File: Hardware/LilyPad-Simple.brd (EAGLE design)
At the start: 50 x 50 mm, 43 parts, among them U1 ATMEGA328P_TQFP, U2 MCP73831, U3 MIC5219 3.3V, Y1 8MHZ

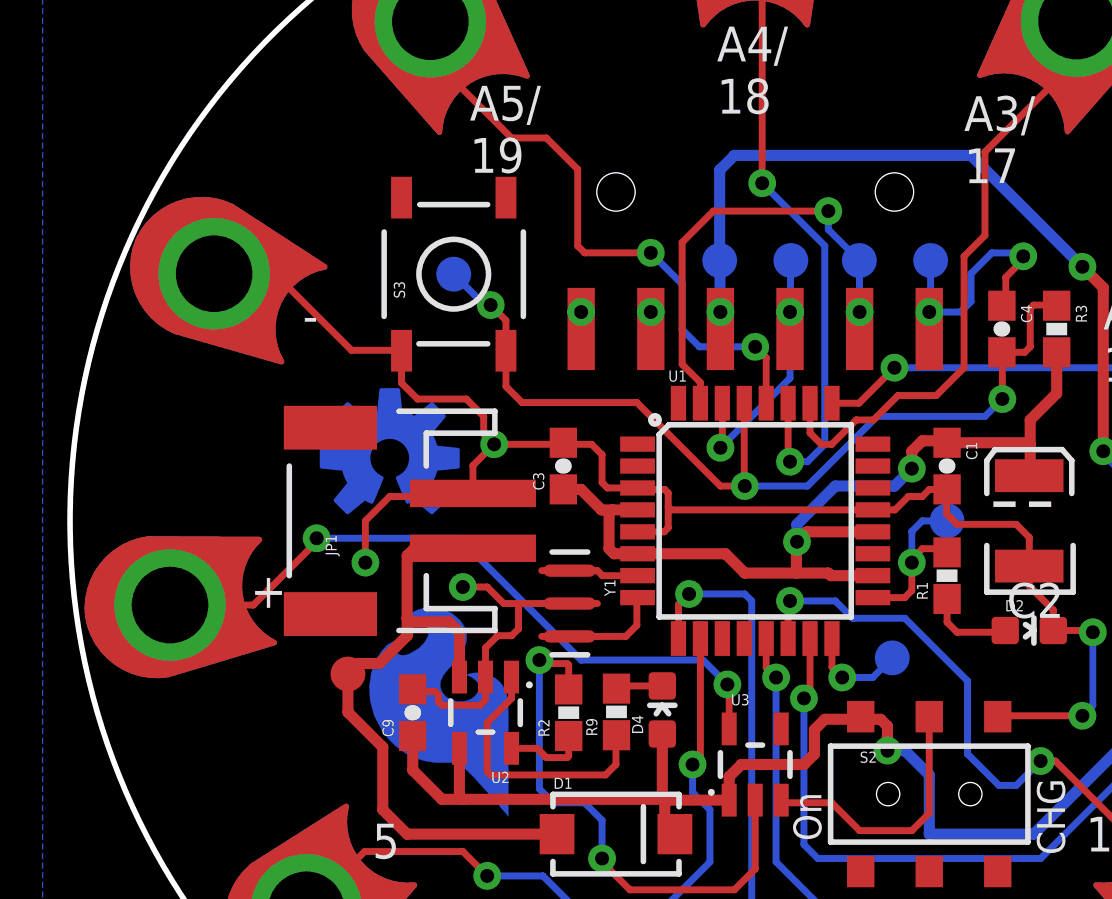
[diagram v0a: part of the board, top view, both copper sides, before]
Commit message: Put test pads on grid, increased trace size on power supply pad
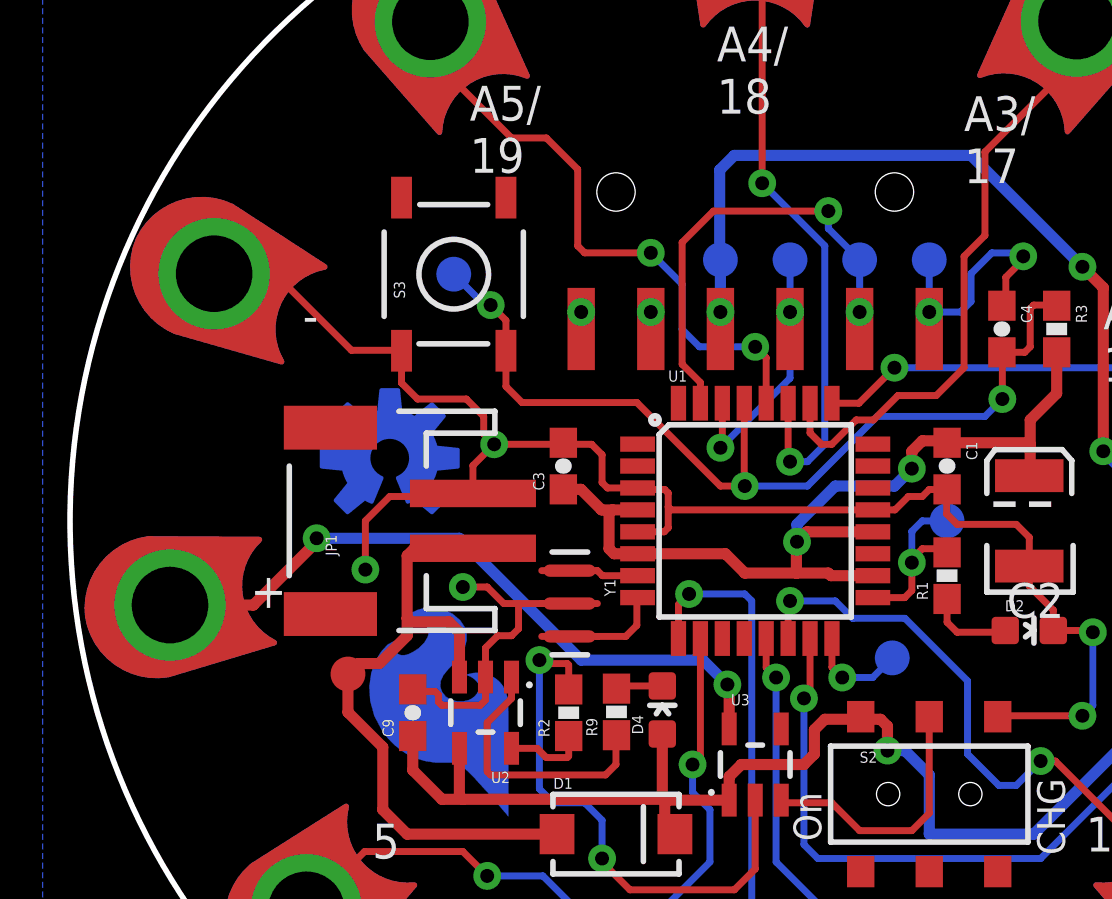
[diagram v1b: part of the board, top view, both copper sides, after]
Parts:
- moved TP-DTR 0.06 mm to (6.35, 9.53)
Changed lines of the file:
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@@
 <layer number="47" name="Measures" color="7" fill="1" visible="no" active="yes"/>
 <layer number="48" name="Document" color="7" fill="1" visible="no" active="yes"/>
-<layer number="49" name="Reference" color="7" fill="1" visible="yes" active="yes"/>
+<layer number="49" name="Reference" color="7" fill="1" visible="no" active="yes"/>
 <layer number="50" name="dxf" color="7" fill="1" visible="no" active="yes"/>
 <layer number="51" name="tDocu" color="6" fill="1" visible="yes" active="yes"/>
@@
 <attribute name="PROD_ID" value="SWCH-08179" x="6.35" y="-9.97" size="1.778" layer="27" display="off"/>
 </element>
-<element name="TP-TX" library="SparkFun" package="PAD.03X.05" value="" x="3.8" y="9.5" rot="MR90"/>
-<element name="TP-RX" library="SparkFun" package="PAD.03X.05" value="" x="1.3" y="9.5" rot="MR0"/>
-<element name="TP-DTR" library="SparkFun" package="PAD.03X.05" value="" x="6.4" y="9.5" rot="MR0"/>
+<element name="TP-TX" library="SparkFun" package="PAD.03X.05" value="" x="3.81" y="9.525" rot="MR90"/>
+<element name="TP-RX" library="SparkFun" package="PAD.03X.05" value="" x="1.27" y="9.525" rot="MR0"/>
+<element name="TP-DTR" library="SparkFun" package="PAD.03X.05" value="" x="6.35" y="9.525" rot="MR0"/>
 <element name="C9" library="SparkFun-Capacitors" package="0603-CAP" value="4.7uF" x="-12.495" y="-7" smashed="yes" rot="R90">
 <attribute name="NAME" x="-13.1935" y="-7.889" size="0.4064" layer="25" rot="R90"/>
@@
 <attribute name="PROD_ID" value="RES-00824" x="-6.806" y="-7" size="1.778" layer="27" rot="R90" display="off"/>
 </element>
-<element name="TP-FTDI_VCC" library="SparkFun" package="PAD.03X.05" value="" x="-1.2954" y="9.4996" rot="MR0"/>
+<element name="TP-FTDI_VCC" library="SparkFun" package="PAD.03X.05" value="" x="-1.27" y="9.525" rot="MR0"/>
 <element name="LOGO2" library="SparkFun-Aesthetics" package="SFE_LOGO_FLAME_COPPER_.3" value="SFE_LOGO_FLAME.3COP" x="-8.509" y="-10.922" rot="MR0"/>
 <element name="LOGO1" library="SparkFun-Aesthetics" package="OSHW-LOGO-M_COPPER" value="OSHW-LOGOM-COPPER" x="-13.335" y="2.286" rot="MR0"/>
@@
 <wire x1="6.35" y1="1.143" x2="6.993" y2="1.143" width="0.254" layer="1"/>
 <wire x1="6.993" y1="1.143" x2="7" y2="1.15" width="0.254" layer="1"/>
-<via x="-14.224" y="-1.524" extent="1-16" drill="0.508"/>
+<via x="-14.224" y="-1.778" extent="1-16" drill="0.508"/>
 <wire x1="-14.224" y1="0" x2="-13.335" y2="0.889" width="0.254" layer="1"/>
 <wire x1="-13.335" y1="0.889" x2="-10.411" y2="0.889" width="0.254" layer="1"/>
@@
 <wire x1="-9.779" y1="-2.413" x2="-10.668" y2="-2.413" width="0.254" layer="1"/>
 <wire x1="-8.636" y1="-3.937" x2="-8.636" y2="-3.016" width="0.254" layer="1"/>
-<wire x1="-14.224" y1="-1.524" x2="-14.224" y2="0" width="0.254" layer="1"/>
+<wire x1="-14.224" y1="-1.778" x2="-14.224" y2="0" width="0.254" layer="1"/>
 <wire x1="-6.806" y1="-6.15" x2="-6.806" y2="-5.259" width="0.254" layer="1"/>
 <wire x1="-6.806" y1="-5.259" x2="-6.858" y2="-5.207" width="0.254" layer="1"/>
@@
 <contactref element="U1" pad="30"/>
 <contactref element="TP-RX" pad="P$1"/>
-<wire x1="1.3" y1="9.5" x2="1.27" y2="7.62" width="0.254" layer="16"/>
 <via x="1.27" y="7.62" extent="1-16" drill="0.508"/>
 <via x="-1.27" y="2.667" extent="1-16" drill="0.508"/>
@@
 <wire x1="-1.2" y1="4.2926" x2="-1.2" y2="2.737" width="0.254" layer="1"/>
 <wire x1="-1.2" y1="2.737" x2="-1.27" y2="2.667" width="0.254" layer="1"/>
+<wire x1="1.27" y1="9.525" x2="1.27" y2="7.62" width="0.254" layer="16"/>
 </signal>
 <signal name="TXO">
@@
 <wire x1="-1.524" y1="11.303" x2="2.667" y2="11.303" width="0.254" layer="1"/>
 <via x="2.667" y="11.303" extent="1-16" drill="0.508"/>
-<wire x1="2.667" y1="11.303" x2="2.667" y2="10.633" width="0.254" layer="16"/>
-<wire x1="3.8" y1="9.5" x2="2.667" y2="10.633" width="0.254" layer="16"/>
-<wire x1="3.8" y1="9.5" x2="3.81" y2="7.62" width="0.254" layer="16"/>
 <via x="3.81" y="7.62" extent="1-16" drill="0.508"/>
 <wire x1="3.81" y1="7" x2="3.81" y2="7.62" width="0.254" layer="1"/>
+<wire x1="3.8" y1="7.63" x2="3.81" y2="7.62" width="0.254" layer="16"/>
+<wire x1="3.81" y1="9.525" x2="3.81" y2="7.62" width="0.254" layer="16"/>
+<wire x1="2.667" y1="11.303" x2="2.667" y2="10.668" width="0.254" layer="16"/>
+<wire x1="2.667" y1="10.668" x2="3.81" y2="9.525" width="0.254" layer="16"/>
 </signal>
 <signal name="D5">
@@
 <contactref element="JP2" pad="1"/>
 <contactref element="TP-DTR" pad="P$1"/>
-<wire x1="6.4" y1="9.5" x2="6.4" y2="7.67" width="0.254" layer="16"/>
 <wire x1="6.4" y1="7.67" x2="6.35" y2="7.62" width="0.254" layer="16"/>
 <via x="6.35" y="7.62" extent="1-16" drill="0.508"/>
@@
 <wire x1="9.144" y1="7.994" x2="9" y2="7.85" width="0.254" layer="1"/>
 <wire x1="6.35" y1="7" x2="6.35" y2="7.62" width="0.254" layer="1"/>
+<wire x1="6.35" y1="9.525" x2="6.35" y2="7.62" width="0.254" layer="16"/>
 </signal>
 <signal name="D6">
@@
 <contactref element="D1" pad="C"/>
 <wire x1="-10.795" y1="-8.3041" x2="-10.791" y2="-8.3001" width="0.254" layer="1"/>
-<wire x1="-1.2954" y1="9.4996" x2="-1.27" y2="7.62" width="0.4064" layer="16"/>
 <via x="-1.27" y="7.62" extent="1-16" drill="0.508"/>
 <wire x1="3.756" y1="-7.239" x2="4.572" y2="-7.239" width="0.4064" layer="1"/>
@@
 <wire x1="12.7" y1="2.54" x2="12.7" y2="8.509" width="0.4064" layer="1"/>
 <wire x1="12.7" y1="8.509" x2="11.938" y2="9.271" width="0.4064" layer="1"/>
-<wire x1="-1.2954" y1="9.4996" x2="-1.2954" y2="12.8016" width="0.4064" layer="16"/>
 <wire x1="-1.2954" y1="12.8016" x2="-0.762" y2="13.335" width="0.4064" layer="16"/>
 <wire x1="-0.762" y1="13.335" x2="7.874" y2="13.335" width="0.4064" layer="16"/>
@@
 <wire x1="10.16" y1="-11.43" x2="13.462" y2="-8.128" width="0.4064" layer="16"/>
 <wire x1="13.462" y1="1.778" x2="13.462" y2="-8.128" width="0.4064" layer="16"/>
+<wire x1="-1.27" y1="9.525" x2="-1.27" y2="7.62" width="0.4064" layer="16"/>
+<wire x1="-1.2954" y1="12.8016" x2="-1.2954" y2="9.5504" width="0.4064" layer="16"/>
+<wire x1="-1.2954" y1="9.5504" x2="-1.27" y2="9.525" width="0.254" layer="16"/>
 </signal>
 <signal name="V_BATT">
@@
 <contactref element="U3" pad="5"/>
 <contactref element="U$45" pad="1"/>
-<wire x1="-21.35230625" y1="-3.07171875" x2="-18.31171875" y2="-3.07171875" width="0.254" layer="1"/>
+<wire x1="-21.35230625" y1="-3.07171875" x2="-18.31171875" y2="-3.07171875" width="0.4064" layer="1"/>
 <via x="-16.002" y="-0.635" extent="1-16" drill="0.508"/>
-<wire x1="-10.795" y1="-0.635" x2="-6.35" y2="-5.08" width="0.254" layer="16"/>
-<wire x1="-6.35" y1="-5.08" x2="-1.905" y2="-5.08" width="0.254" layer="16"/>
-<wire x1="-1.905" y1="-5.08" x2="-1.016" y2="-5.969" width="0.254" layer="16"/>
+<wire x1="-1.905" y1="-5.08" x2="-1.016" y2="-5.969" width="0.4064" layer="16"/>
 <via x="-1.016" y="-5.969" extent="1-16" drill="0.508"/>
 <wire x1="-16.002" y1="-0.635" x2="-16.002" y2="-0.762" width="0.254" layer="1"/>
-<wire x1="-16.002" y1="-0.762" x2="-18.31171875" y2="-3.07171875" width="0.254" layer="1"/>
-<wire x1="-16.002" y1="-0.635" x2="-10.795" y2="-0.635" width="0.254" layer="16"/>
-<wire x1="-0.95" y1="-7.5899" x2="-0.95" y2="-6.035" width="0.254" layer="1"/>
+<wire x1="-16.002" y1="-0.762" x2="-18.31171875" y2="-3.07171875" width="0.4064" layer="1"/>
+<wire x1="-16.002" y1="-0.635" x2="-10.795" y2="-0.635" width="0.4064" layer="16"/>
+<wire x1="-0.95" y1="-7.5899" x2="-0.95" y2="-6.035" width="0.4064" layer="1"/>
 <wire x1="-0.95" y1="-6.035" x2="-1.016" y2="-5.969" width="0.254" layer="1"/>
+<wire x1="-1.905" y1="-5.08" x2="-6.35" y2="-5.08" width="0.4064" layer="16"/>
+<wire x1="-6.35" y1="-5.08" x2="-10.795" y2="-0.635" width="0.4064" layer="16"/>
 </signal>
 <signal name="N$5">

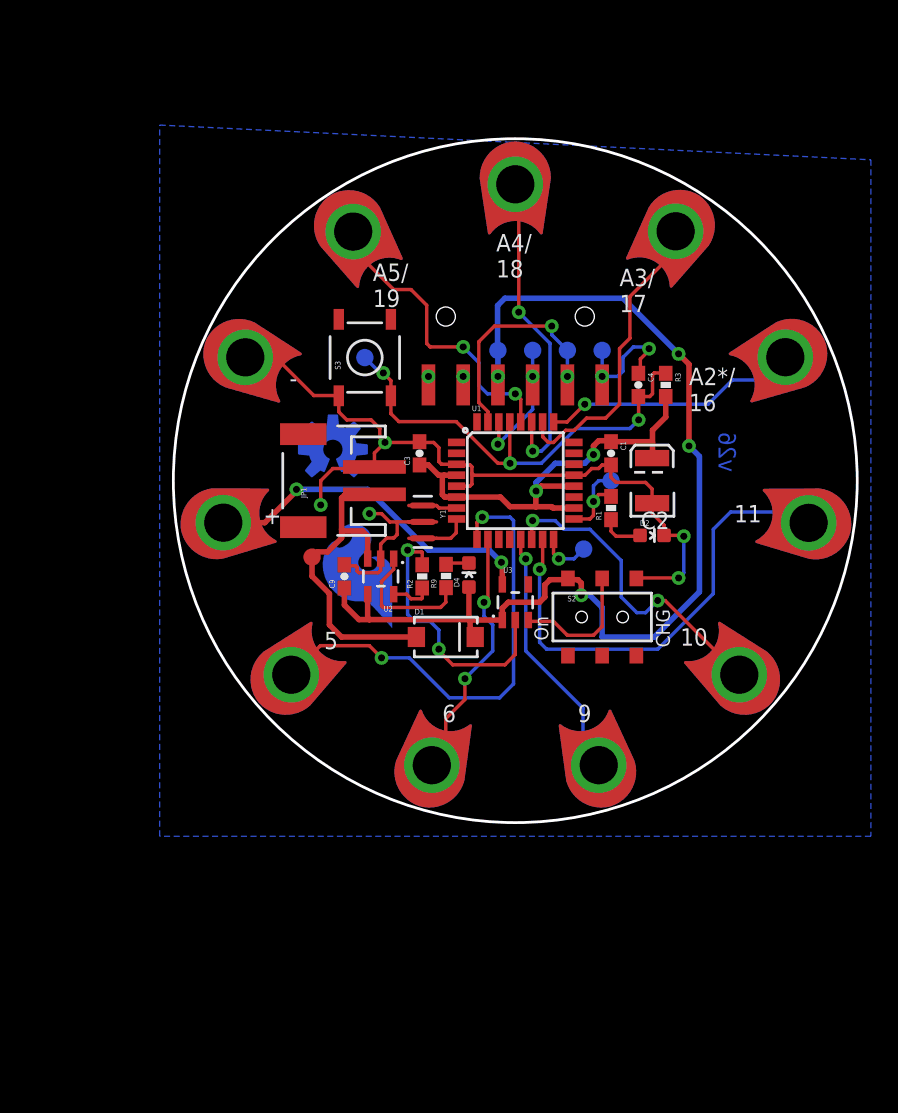
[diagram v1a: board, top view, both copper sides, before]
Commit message: DRC changes, fixed some errors
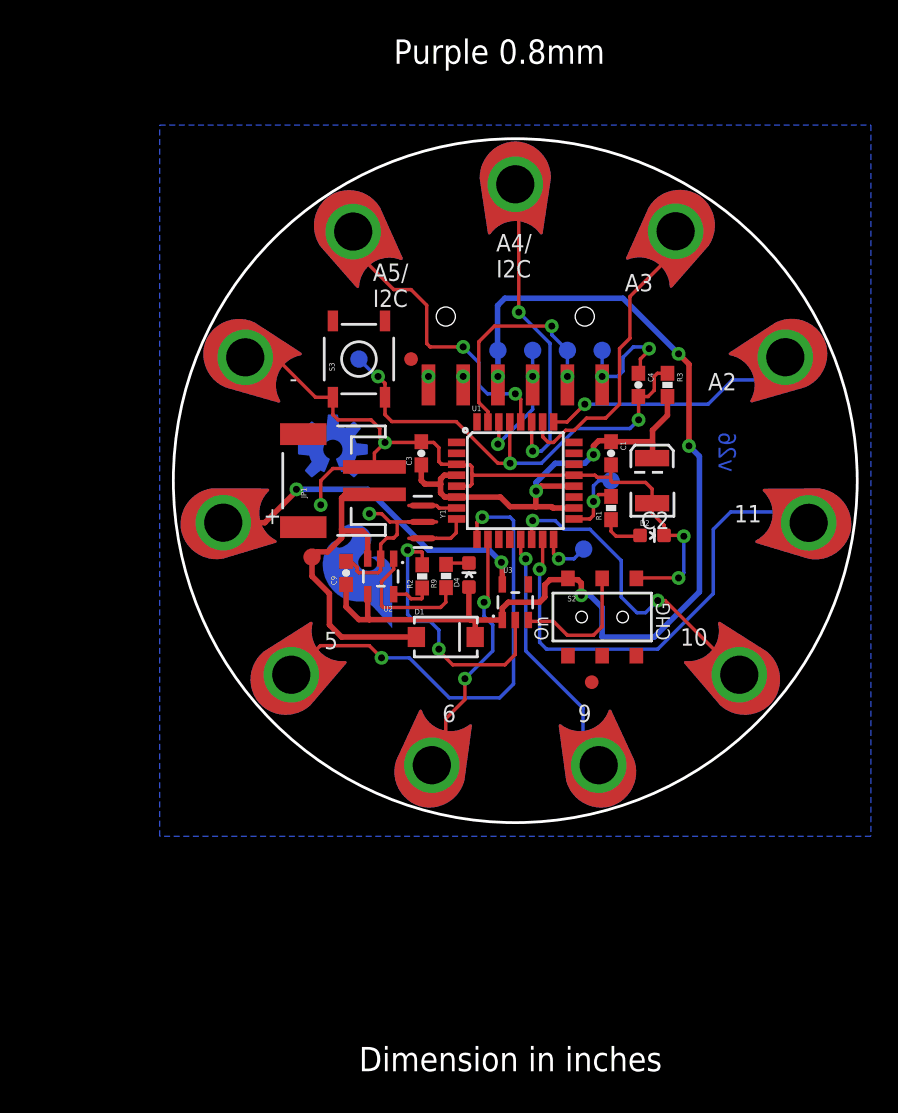
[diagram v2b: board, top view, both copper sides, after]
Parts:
- added FID1, FID2: FIDUCIAL1X2, SparkFun-Aesthetics:FIDUCIAL-1X2
- added U$2: LOGO-LPLPA, LilyPad-Wearables:LOGO-LPA
- D4: value Yellow -> RED
- moved PP-RST 0.44 mm to (-11.4, 8.89)
- moved S3 0.44 mm to (-11.4, 8.89)
- moved C9 0.28 mm to (-12.4, -6.75)
- moved R3 0.13 mm to (11.1, 7.00)
- moved C3 0.13 mm to (-6.87, 2.00)
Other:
- board text added: "A2"
- board text added: "A3"
- board text added: "A4/ I2C"
- board text added: "A5/ I2C"
- board text added: "Dimension in inches"
- board text added: "Purple 0.8mm"
- board text removed: "A2*/ 16"
- board text removed: "A3/ 17"
- board text removed: "A4/ 18"
- board text removed: "A5/ 19"

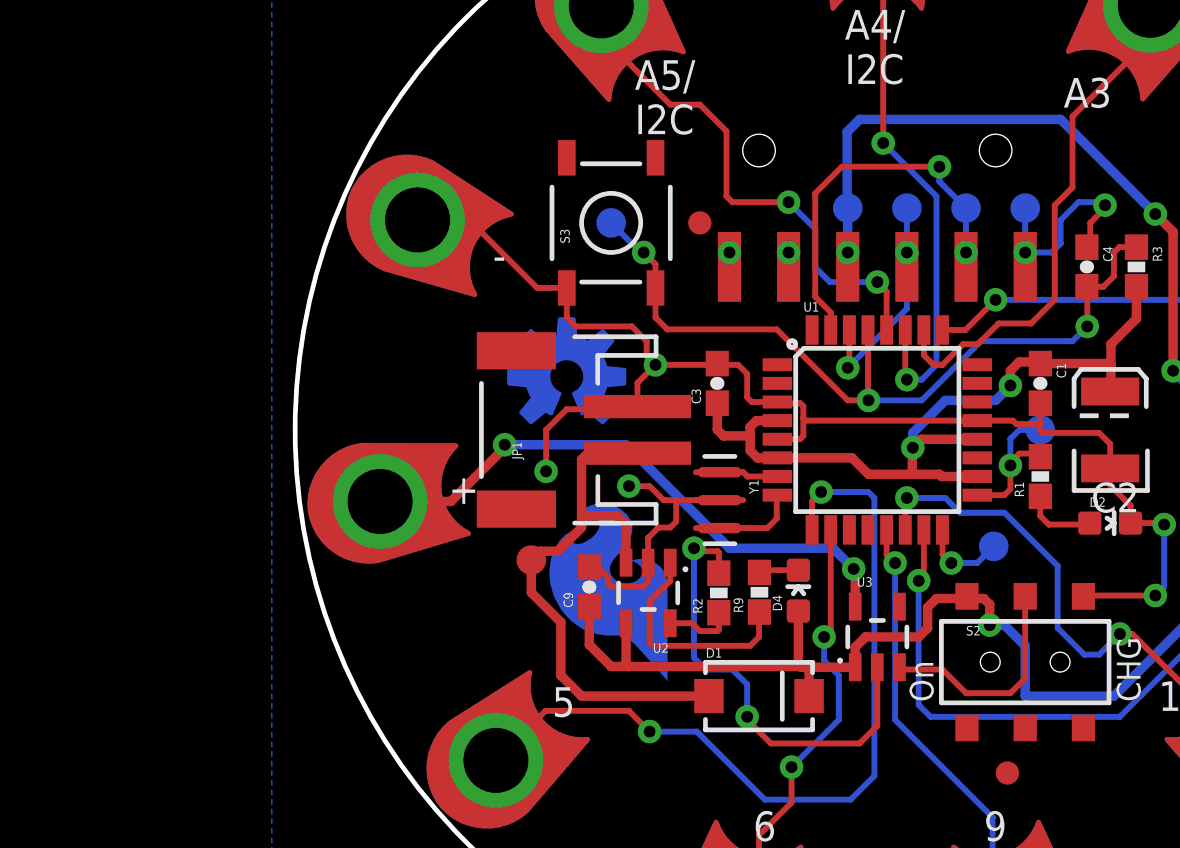
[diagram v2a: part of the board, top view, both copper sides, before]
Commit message: Change to 3.3v connections
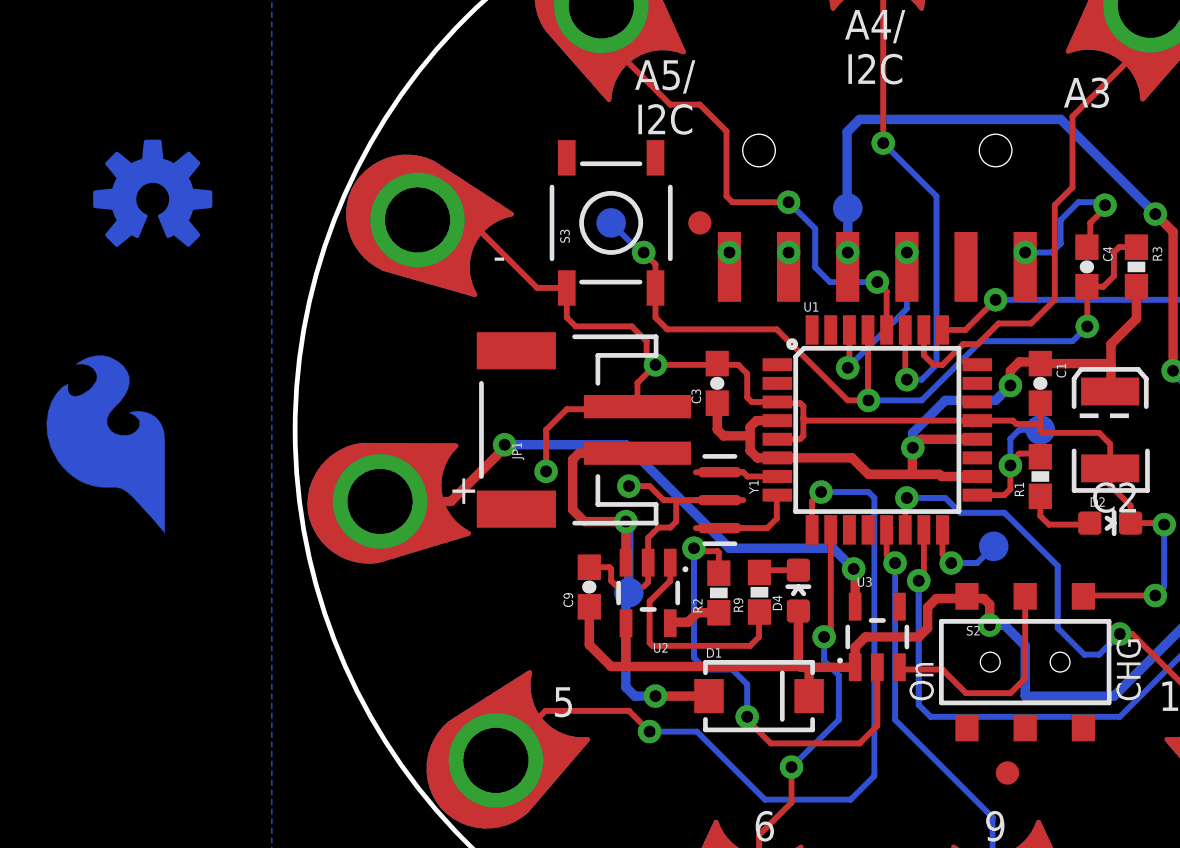
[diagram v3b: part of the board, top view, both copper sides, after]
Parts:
- removed TP-DTR, TP-RX, TP-TX: (no value), SparkFun:PAD.03X.05
- moved LOGO2 22.5 mm to (-30.1, -4.57)
- moved LOGO1 19.3 mm to (-31.1, 9.91)
- moved TP-VBATT1 4.42 mm to (-10.7, -6.99), flipped to the bottom
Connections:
- removed net VCC: C1.1, C2.A, C3.1, R3.2, U1.18, U1.20, U1.4, U1.6
- net 3.3V: now also C1.1, C2.A, C3.1, R3.2, U1.18, U1.20, U1.4, U1.6
- net DTR: no longer JP2.1, TP-DTR.P$1
- net RXI: no longer JP2.3, TP-RX.P$1
- net TXO: no longer JP2.2, TP-TX.P$1
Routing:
- net VCC: track 35.0 -> 0.00 mm, vias 2 -> 0
- net 3.3V: track 25.3 -> 60.3 mm, vias 2 -> 4
- net TXO: track 16.7 -> 0.00 mm, vias 2 -> 0
- net V_BATT: track 24.1 -> 20.3 mm, vias 0 -> 2
- net RXI: track 10.2 -> 7.66 mm
- net DTR: track 9.69 -> 7.17 mm
- net GND: track 93.1 -> 92.1 mm
- net N$6: track 2.98 -> 2.27 mm
